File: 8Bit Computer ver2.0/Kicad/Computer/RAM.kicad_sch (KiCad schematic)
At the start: 8 parts, among them IC216 SN74F521DWR, IC217 SN74F521DWR, IC218 SN74LVC1G14DBVR, IC219 SN74LVC1G14DBVR, IC220 SN74LVC1G14DBVR, IC221 SN74AHC74DR, IC222 SN74LVC1G14DBVR, IC223 AS7C1024B-12TCN

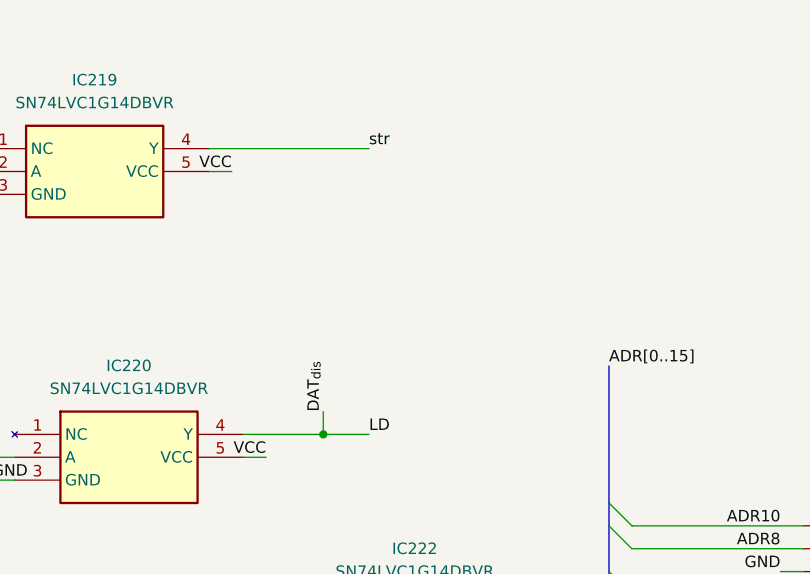
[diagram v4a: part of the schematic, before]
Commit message: Kicad Fixes only schematic
fixed important schematic errors
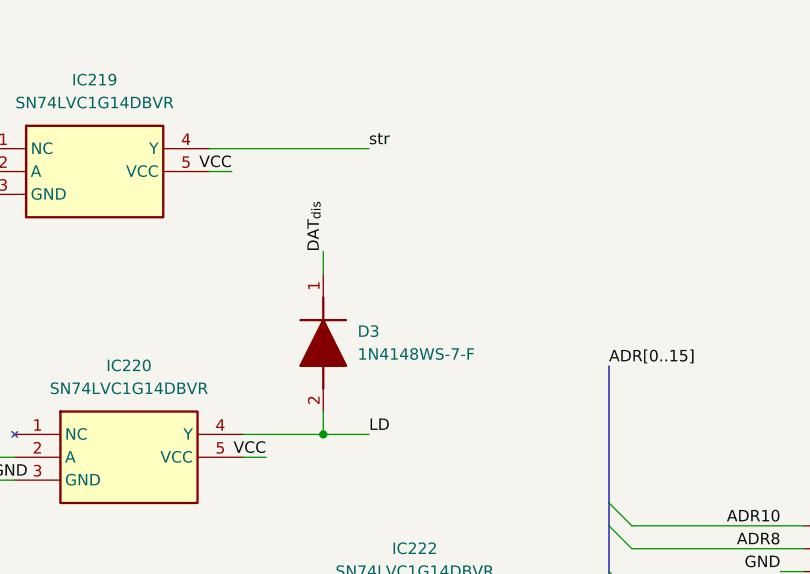
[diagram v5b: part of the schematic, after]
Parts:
- added D3: 1N4148WS-7-F, Samacsys:SOD2513X120N, symbol Samacsys:1N4148WS-7-F
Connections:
- net DAT_{dis}: now also D3.1 (K); no longer IC220.4 (Y), IC221.2 (1D)
- new net LD: D3.2 (A), IC220.4 (Y), IC221.2 (1D)
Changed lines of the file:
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@@
 	(wire
 		(pts
+			(xy 162.56 53.34) (xy 162.56 55.88)
+		)
+		(stroke
+			(width 0)
+			(type default)
+		)
+	)
+	(wire
+		(pts
 			(xy 153.67 133.35) (xy 151.13 133.35)
 		)
@@
 		)
 	)
+	(label "DAT_{dis}"
+		(at 162.56 53.34 90)
+		(effects
+			(font
+				(size 1.27 1.27)
+			)
+			(justify left bottom)
+		)
+	)
 	(label "CMD0"
 		(at 73.66 80.01 180)
@@
 		)
 	)
-	(label "DAT_{dis}"
-		(at 162.56 71.12 90)
-		(effects
-			(font
-				(size 1.27 1.27)
-			)
-			(justify left bottom)
-		)
-	)
 	(label "CMD7"
 		(at 109.22 85.09 0)
@@
 					(unit 1)
 				)
+			)
+		)
+	)
+	(symbol
+		(lib_id "Samacsys:1N4148WS-7-F")
+		(at 162.56 55.88 270)
+		(unit 1)
+		(exclude_from_sim no)
+		(in_bom yes)
+		(on_board yes)
+		(dnp no)
+		(fields_autoplaced yes)
+		(property "Reference" "D3"
+			(at 166.37 62.2299 90)
+			(effects
+				(font
+					(size 1.27 1.27)
+				)
+				(justify left)
+			)
+		)
+		(property "Value" "1N4148WS-7-F"
+			(at 166.37 64.7699 90)
+			(effects
+				(font
+					(size 1.27 1.27)
+				)
+				(justify left)
+			)
+		)
+		(property "Footprint" "Samacsys:SOD2513X120N"
+			(at 65.1 67.31 0)
+			(effects
+				(font
+					(size 1.27 1.27)
+				)
+				(justify left top)
+				(hide yes)
+			)
+		)
+		(property "Datasheet" "https://www.diodes.com//assets/Datasheets/1N4148WS_BAV16WS.pdf"
+			(at -34.9 67.31 0)
+			(effects
+				(font
+					(size 1.27 1.27)
+				)
+				(justify left top)
+				(hide yes)
+			)
+		)
+		(property "Description" "Diode Switching 150mA 75V 200mW SOD323 Diodes Inc 1N4148WS-7-F Switching Diode, 150mA 75V, 2-Pin SOD-323"
+			(at 162.56 55.88 0)
+			(effects
+				(font
+					(size 1.27 1.27)
+				)
+				(hide yes)
+			)
+		)
+		(property "Height" "1.2"
+			(at -234.9 67.31 0)
+			(effects
+				(font
+					(size 1.27 1.27)
+				)
+				(justify left top)
+				(hide yes)
+			)
+		)
+		(property "Mouser Part Number" "621-1N4148WS-F"
+			(at -334.9 67.31 0)
+			(effects
+				(font
+					(size 1.27 1.27)
+				)
+				(justify left top)
+				(hide yes)
+			)
+		)
+		(property "Mouser Price/Stock" "https://www.mouser.co.uk/ProductDetail/Diodes-Incorporated/1N4148WS-7-F?qs=4drIV0IxA0r8aNy7%2Fu4kVw%3D%3D"
+			(at -434.9 67.31 0)
+			(effects
+				(font
+					(size 1.27 1.27)
+				)
+				(justify left top)
+				(hide yes)
+			)
+		)
+		(property "Manufacturer_Name" "Diodes Incorporated"
+			(at -534.9 67.31 0)
+			(effects
+				(font
+					(size 1.27 1.27)
+				)
+				(justify left top)
+				(hide yes)
+			)
+		)
+		(property "Manufacturer_Part_Number" "1N4148WS-7-F"
+			(at -634.9 67.31 0)
+			(effects
+				(font
+					(size 1.27 1.27)
+				)
+				(justify left top)
+				(hide yes)
+			)
+		)
+		(pin "1"
+		)
+		(pin "2"
+		)
+		(instances
+			(project "Computer"
+				(path "/1196a00e-6878-4d6d-82b7-9e052dfe7c14/42d222c2-85ce-47c7-bf35-977080c4de05"
+					(reference "D3")
+					(unit 1)
+				)

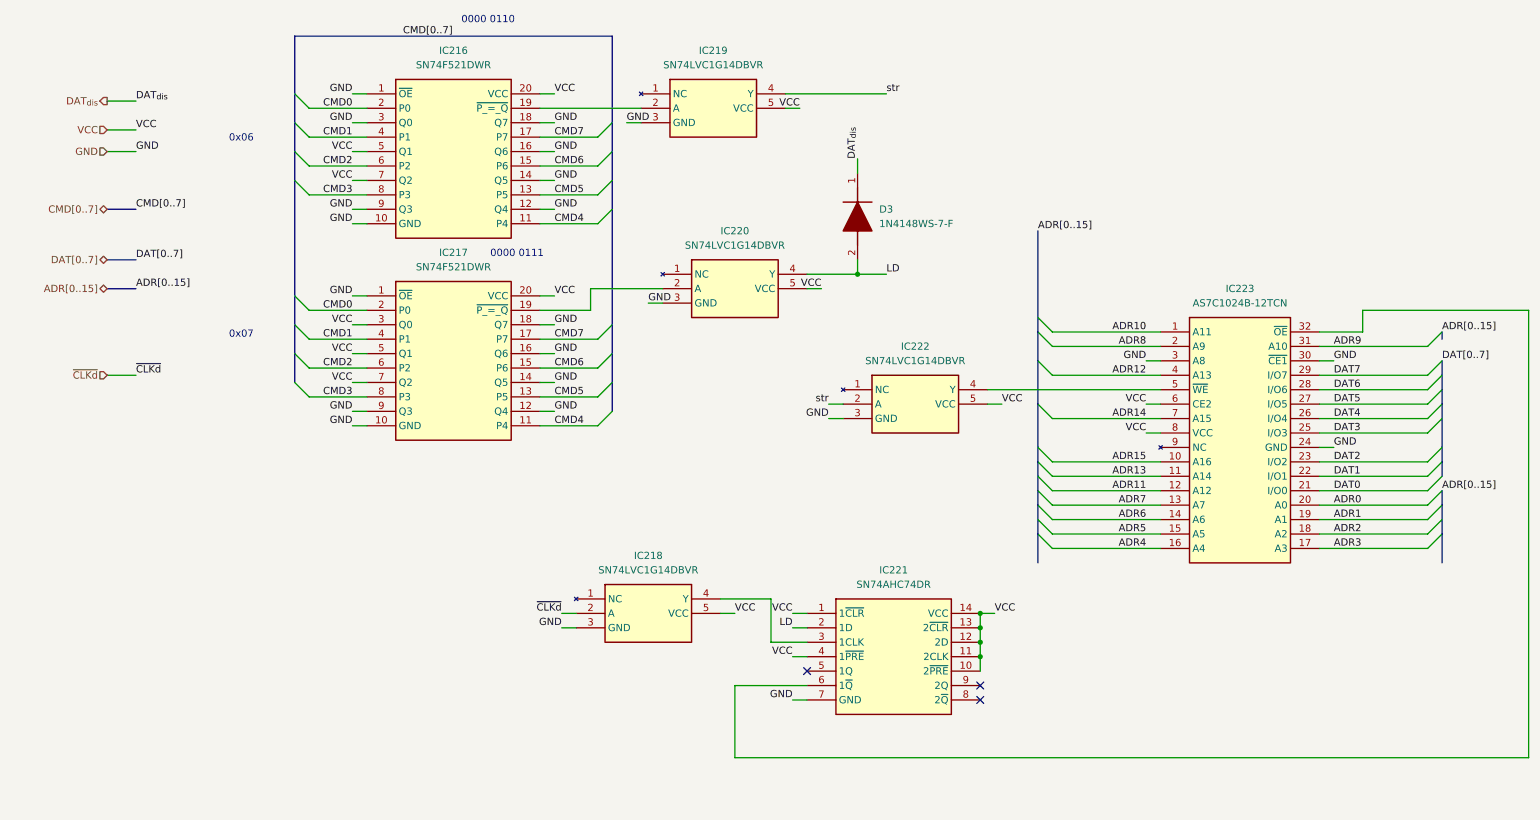
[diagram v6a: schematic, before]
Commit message: Kicad
fixed some design errors(dat dis DistShiftreg, wrong cmd pins)
added description to every CMD for better debug, use CTRL+f and use option "Whole words only" to search e.g. inc
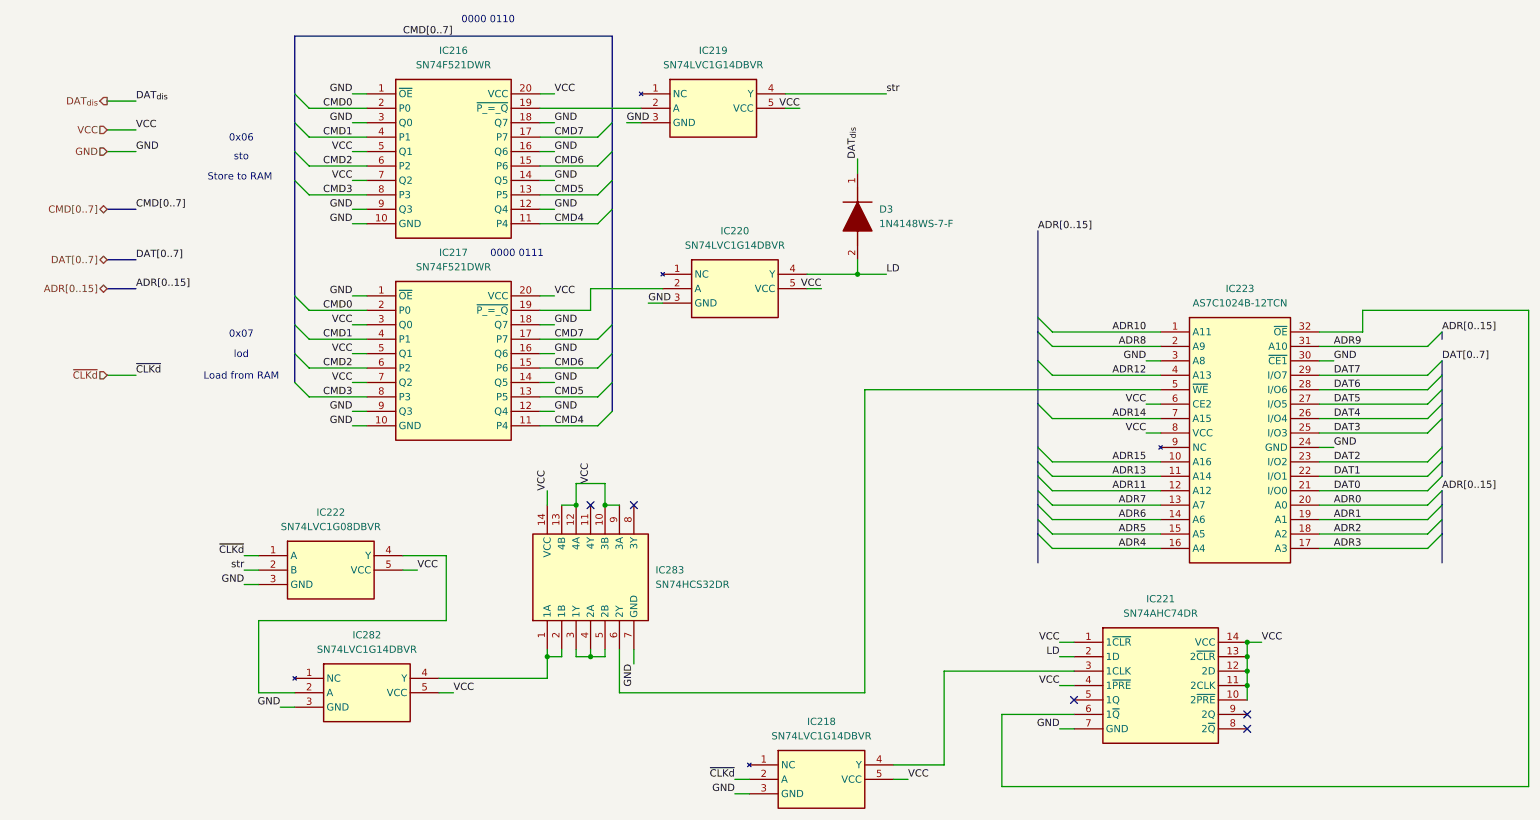
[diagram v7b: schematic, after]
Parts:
- removed IC222: SN74LVC1G14DBVR, Samacsys:SOT95P280X145-5N, symbol Samacsys:SN74LVC1G14DBVR
- added IC222: SN74LVC1G08DBVR, Samacsys:SOT95P280X145-5N, symbol Samacsys:SN74LVC1G08DBVR
- added IC282: SN74LVC1G14DBVR, Samacsys:SOT95P280X145-5N, symbol Samacsys:SN74LVC1G14DBVR
- added IC283: SN74HCS32DR, Samacsys:SOIC127P600X175-14N, symbol Samacsys:SN74HCS32DR
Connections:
- net GND: now also IC222.3 (GND), IC282.3 (GND), IC283.7 (GND)
- net VCC: now also IC222.5 (VCC), IC282.5 (VCC), IC283.10 (3B), IC283.12 (4A), IC283.13 (4B), IC283.14 (VCC), IC283.9 (3A)
- net str: now also IC222.2 (B)
- net ~{CLKd}: now also IC222.1 (A)
- net at IC223.5 (~{WE}): now also IC283.6 (2Y)
- new net: IC222.4 (Y), IC282.2 (A)
- new net: IC282.4 (Y), IC283.1 (1A), IC283.2 (1B)
- new net: IC283.3 (1Y), IC283.4 (2A), IC283.5 (2B)
- no-connect marks 3 -> 5
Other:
- note added: "Load from RAM"
- note added: "Store to RAM"
- note added: "lod"
- note added: "sto"
- moved on the sheet: IC218, IC221

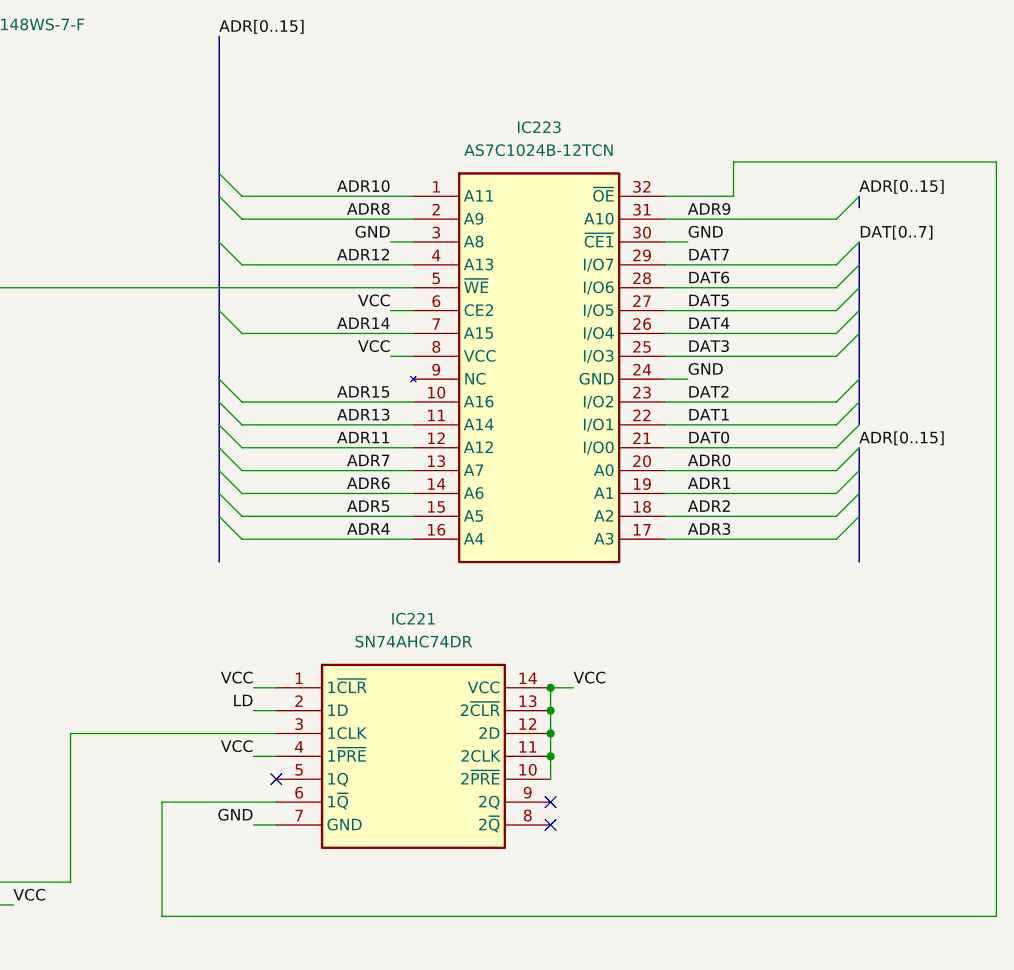
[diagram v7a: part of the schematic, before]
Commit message: part 1 of changing to A4
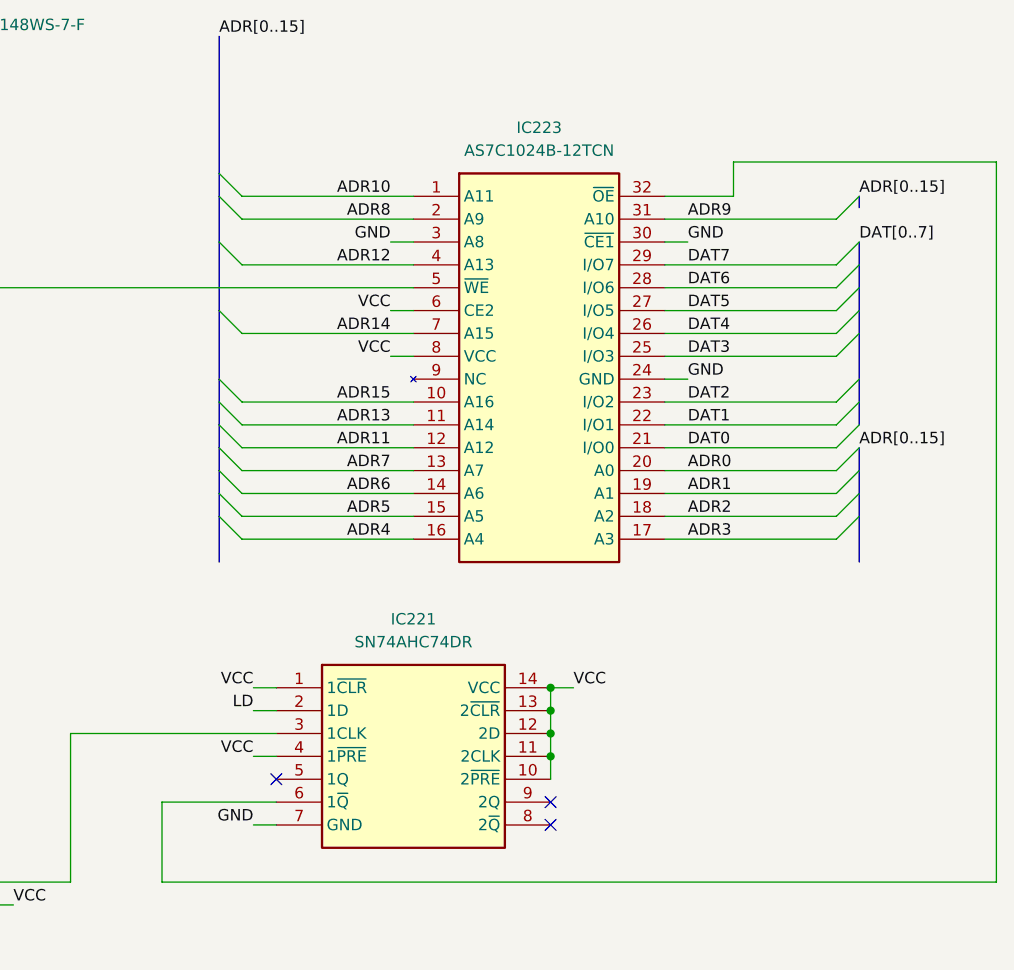
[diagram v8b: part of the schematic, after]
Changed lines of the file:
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@@
 	(wire
 		(pts
-			(xy 187.96 163.83) (xy 280.67 163.83)
+			(xy 187.96 160.02) (xy 280.67 160.02)
 		)
 		(stroke
@@
 	(wire
 		(pts
-			(xy 187.96 151.13) (xy 187.96 163.83)
+			(xy 187.96 151.13) (xy 187.96 160.02)
 		)
 		(stroke
@@
 	(wire
 		(pts
-			(xy 280.67 80.01) (xy 280.67 163.83)
-		)
-		(stroke
+			(xy 280.67 80.01) (xy 280.67 160.02)
+		)
+		(stroke
